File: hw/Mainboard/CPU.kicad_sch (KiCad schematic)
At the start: 8 parts, among them U11 W65C02S, U12 AS6C1008

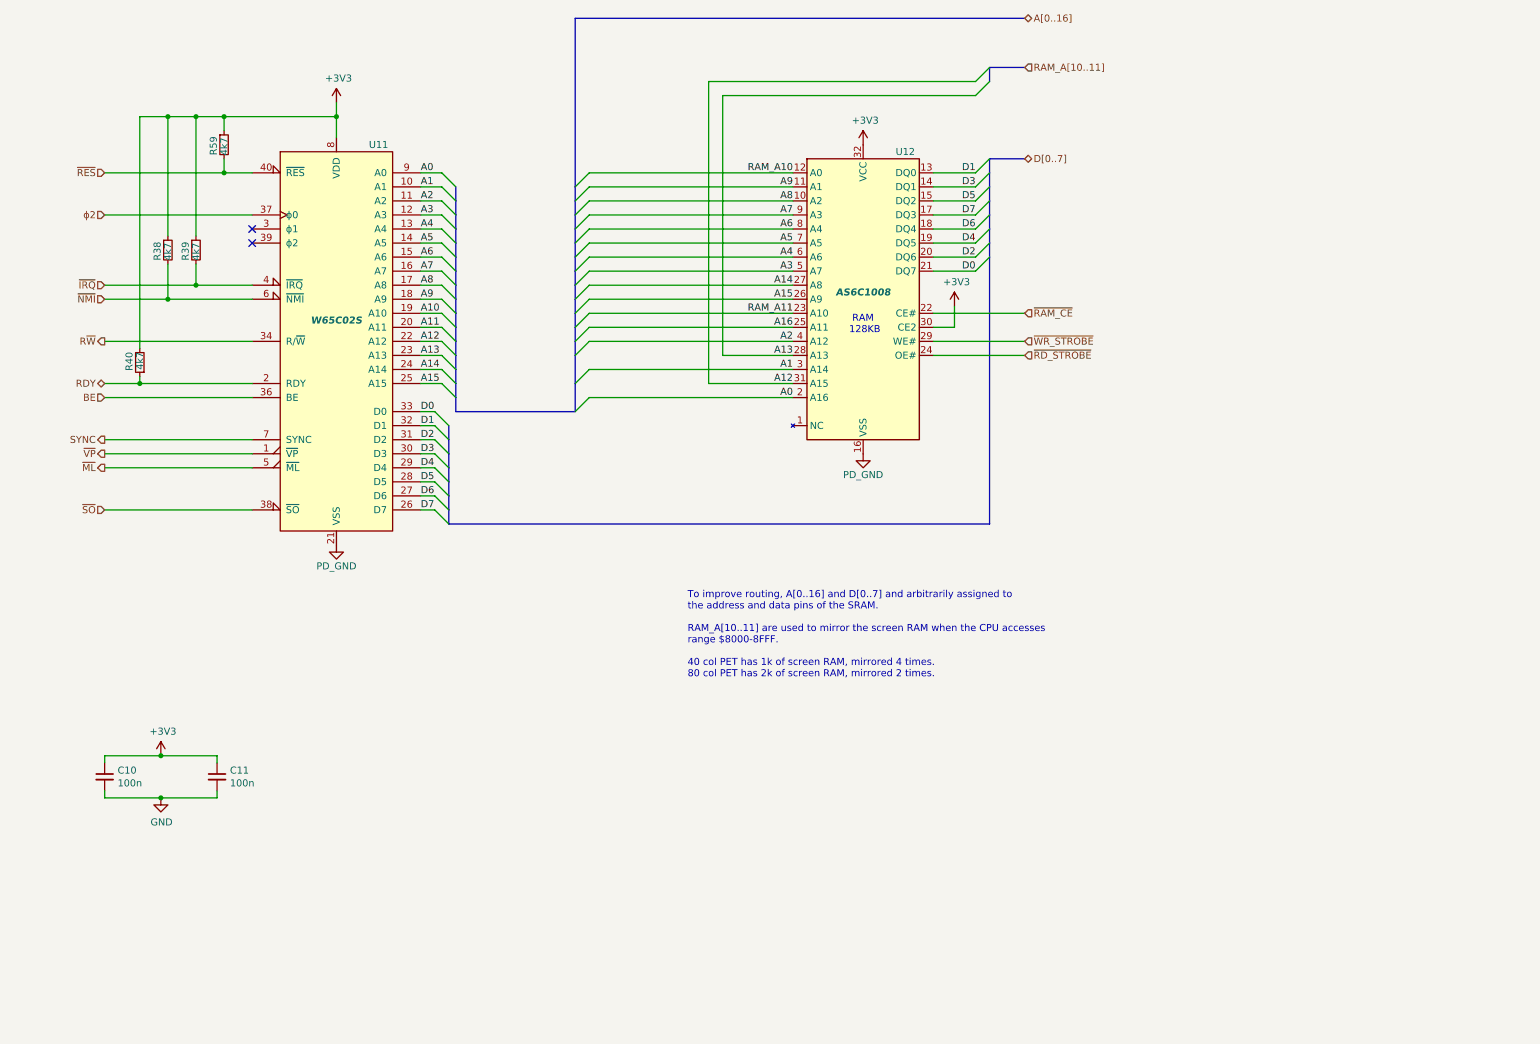
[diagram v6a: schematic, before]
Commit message: hw: larger schematic pages, routed w/netties
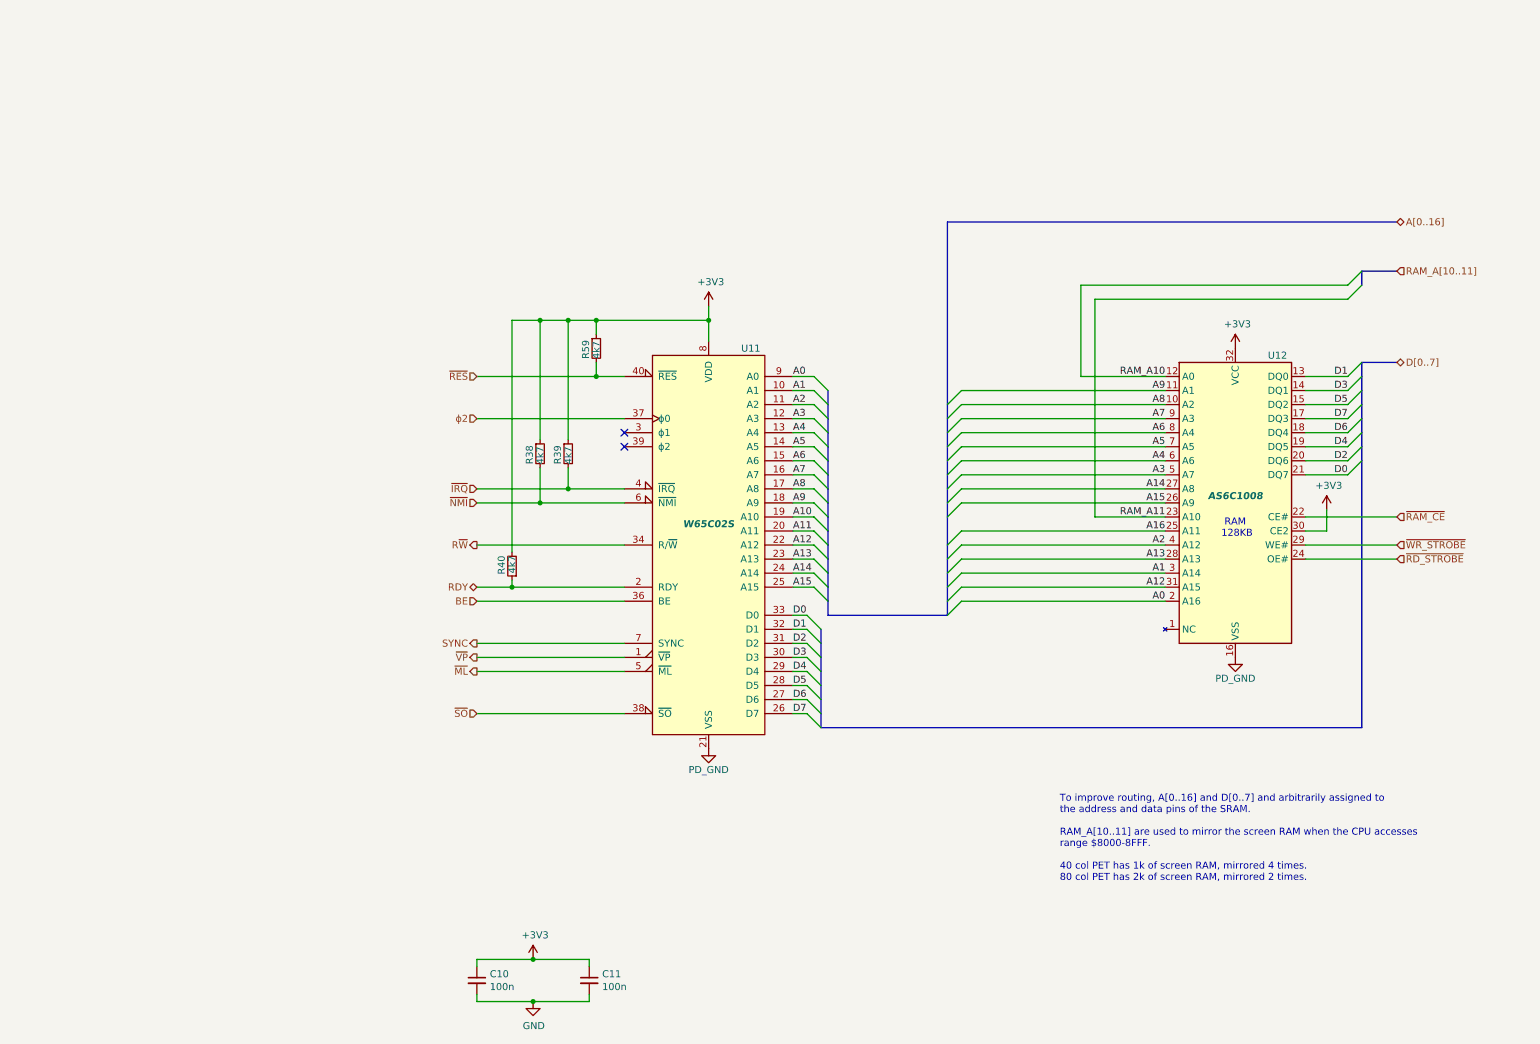
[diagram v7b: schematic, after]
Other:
- moved on the sheet: C10, C11, R38, R39, R40, R59, U11, U12

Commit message: hw: wip
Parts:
- added PT1, PT2: PowerTie_2, PET:NetTie-2_SMD_Pad_1.6_to_0.4mm, symbol PET:PowerTie_2
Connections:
- net +3V3: no longer names the net of C10.1, R38.1, R39.1, R40.2, R59.1
- net +3V3: now also PT1.2; no longer C11.1, U11.8 (VDD), U12.30 (CE2), U12.32 (VCC)
- new net: C11.1, PT2.2, U12.30 (CE2)
- new net PD_3V3: PT1.1, PT2.1, U11.8 (VDD), U12.32 (VCC)
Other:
- moved on the sheet: C10, C11
